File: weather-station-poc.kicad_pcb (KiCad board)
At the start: 4 copper layers, 165 x 91.2 mm, 136 parts, among them IC1 632723100011, IC2 TCPP01-M12, IC3 USBLC6-2SC6, IC4 BME690, IC5 S2-LPQTR, IC6 BALF-SPI2-01D3, IC7 STSAFA110S8OCD03, J1 Conn_ARM_JTAG_SWD_10, J2 61300311121, J3 61300311121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

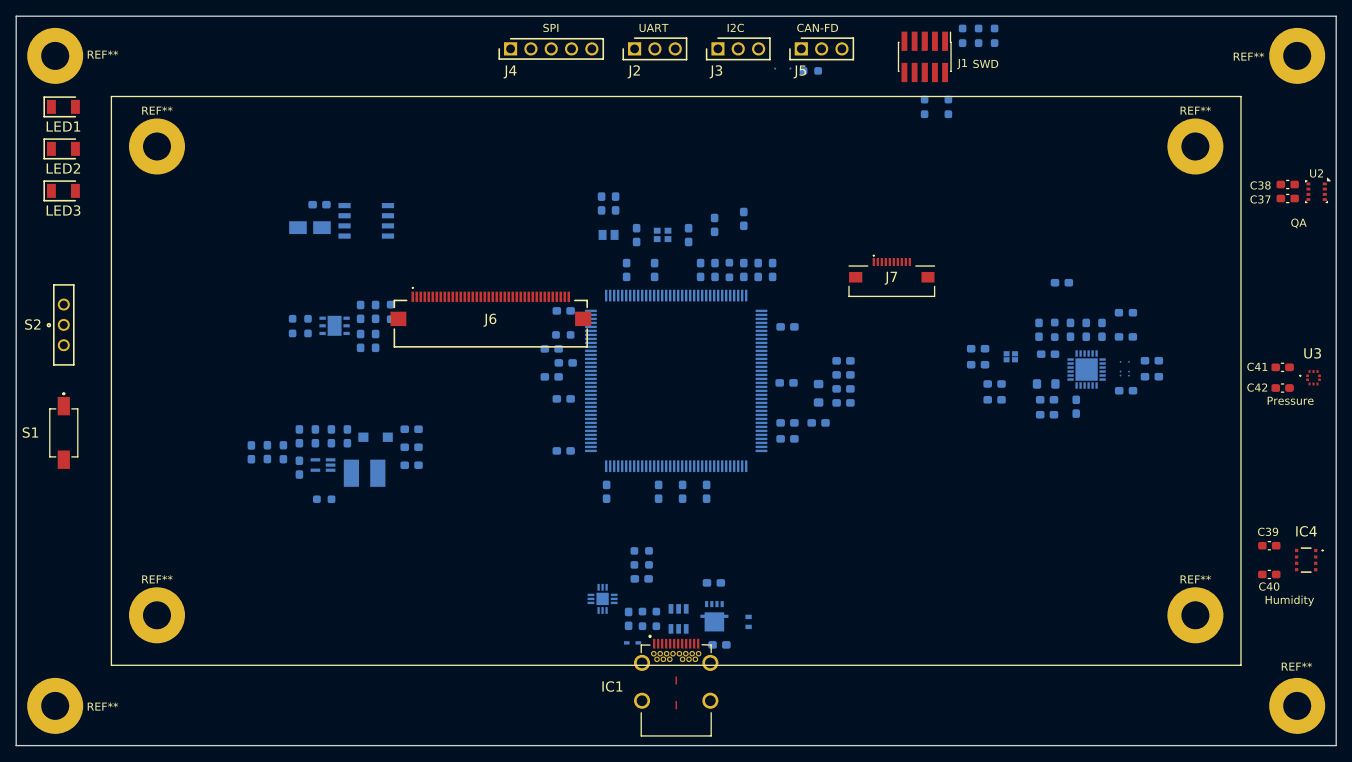
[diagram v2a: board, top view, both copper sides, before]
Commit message: Modify USB data signals name to trace diff pairs
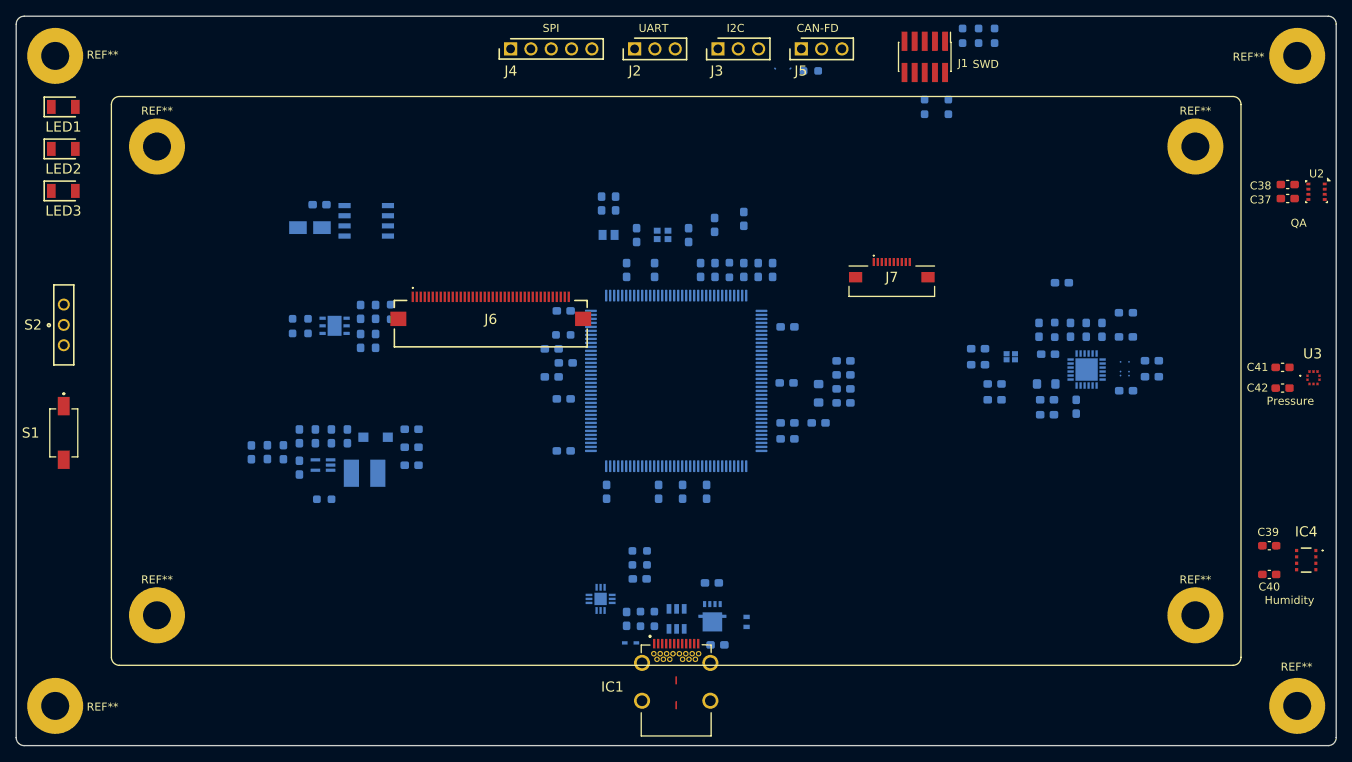
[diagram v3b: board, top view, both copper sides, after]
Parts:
- moved C1 0.25 mm to (141.1, 116.2)
- moved C2 0.25 mm to (150.9, 124.5)
- moved C3 0.25 mm to (150.2, 116.8)
- moved C4 0.25 mm to (139.5, 121.2)
- moved D1 0.25 mm to (154.5, 121.6)
- moved D2 0.25 mm to (140.0, 124.2)
- moved IC2 0.25 mm to (136.2, 118.8)
- moved IC3 0.25 mm to (145.8, 121.2)
- moved Q1 0.25 mm to (150.2, 120.9)
- moved R1 0.25 mm to (143.0, 121.2)
- moved R2 0.25 mm to (141.2, 121.2)
- moved R3 0.25 mm to (141.1, 114.5)
- moved R4 0.25 mm to (141.1, 112.8)
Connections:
- net /MCU/DN_MCU renamed /MCU/MCU_DN
- net /MCU/DP_MCU renamed /MCU/MCU_DP
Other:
- outline, holes or cut-outs redrawn
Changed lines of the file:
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@@
 	(net 41 "Net-(IC2-VBUS_CTRL)")
 	(net 42 "/MCU/~{FLT}_MCU")
-	(net 43 "/MCU/DN_MCU")
-	(net 44 "/MCU/DP_MCU")
+	(net 43 "/MCU/MCU_DN")
+	(net 44 "/MCU/MCU_DP")
 	(net 45 "unconnected-(IC3-VBUS-Pad5)")
 	(net 46 "/Debug-boot/SCL_Debug")
@@
 	(footprint "weather-station-poc-fp:ESDA25P351U1M"
 		(layer "B.Cu")
-		(at 154.75 121.625 -90)
+		(at 154.5 121.625 -90)
 		(descr "1610_2023")
 		(tags "TVS Diode (Uni-directional)")
@@
 	(footprint "weather-station-poc-fp:QFN50P300X300X100-13N-D"
 		(layer "B.Cu")
-		(at 136.5 118.75 -90)
+		(at 136.25 118.75 -90)
 		(descr "QFN12")
 		(tags "Integrated Circuit")
@@
 	(footprint "Capacitor_SMD:C_0603_1608Metric_Pad1.08x0.95mm_HandSolder"
 		(layer "B.Cu")
-		(at 141.3875 116.25 180)
+		(at 141.1375 116.25 180)
 		(descr "Capacitor SMD 0603 (1608 Metric), square (rectangular) end terminal, IPC-7351 nominal with elongated pad for handsoldering. (Body size source: IPC-SM-782 page 76, https://www.pcb-3d.com/wordpress/wp-content/uploads/ipc-sm-782a_amendment_1_and_2.pdf), generated with kicad-footprint-generator")
 		(tags "capacitor handsolder")
@@
 	(footprint "weather-station-poc-fp:STL20N6F7"
 		(layer "B.Cu")
-		(at 150.475 120.925)
+		(at 150.225 120.925)
 		(descr "PowerFLAT™ 3.3x3.3")
 		(tags "MOSFET (N-Channel)")
@@
 	(footprint "Resistor_SMD:R_0603_1608Metric_Pad0.98x0.95mm_HandSolder"
 		(layer "B.Cu")
-		(at 141.3875 114.5)
+		(at 141.1375 114.5)
 		(descr "Resistor SMD 0603 (1608 Metric), square (rectangular) end terminal, IPC-7351 nominal with elongated pad for handsoldering. (Body size source: IPC-SM-782 page 72, https://www.pcb-3d.com/wordpress/wp-content/uploads/ipc-sm-782a_amendment_1_and_2.pdf), generated with kicad-footprint-generator")
 		(tags "resistor handsolder")
@@
 	(footprint "Resistor_SMD:R_0603_1608Metric_Pad0.98x0.95mm_HandSolder"
 		(layer "B.Cu")
-		(at 143.22 121.25 -90)
+		(at 142.97 121.25 -90)
 		(descr "Resistor SMD 0603 (1608 Metric), square (rectangular) end terminal, IPC-7351 nominal with elongated pad for handsoldering. (Body size source: IPC-SM-782 page 72, https://www.pcb-3d.com/wordpress/wp-content/uploads/ipc-sm-782a_amendment_1_and_2.pdf), generated with kicad-footprint-generator")
 		(tags "resistor handsolder")
@@
 	(footprint "weather-station-poc-fp:SODFL1608X70N"
 		(layer "B.Cu")
-		(at 140.245 124.25)
+		(at 139.995 124.25)
 		(descr "SOD-523")
 		(tags "Diode")
@@
 	(footprint "Resistor_SMD:R_0603_1608Metric_Pad0.98x0.95mm_HandSolder"
 		(layer "B.Cu")
-		(at 141.3875 112.75 180)
+		(at 141.1375 112.75 180)
 		(descr "Resistor SMD 0603 (1608 Metric), square (rectangular) end terminal, IPC-7351 nominal with elongated pad for handsoldering. (Body size source: IPC-SM-782 page 72, https://www.pcb-3d.com/wordpress/wp-content/uploads/ipc-sm-782a_amendment_1_and_2.pdf), generated with kicad-footprint-generator")
 		(tags "resistor handsolder")
@@
 	(footprint "Resistor_SMD:R_0603_1608Metric_Pad0.98x0.95mm_HandSolder"
 		(layer "B.Cu")
-		(at 141.485 121.25 -90)
+		(at 141.235 121.25 -90)
 		(descr "Resistor SMD 0603 (1608 Metric), square (rectangular) end terminal, IPC-7351 nominal with elongated pad for handsoldering. (Body size source: IPC-SM-782 page 72, https://www.pcb-3d.com/wordpress/wp-content/uploads/ipc-sm-782a_amendment_1_and_2.pdf), generated with kicad-footprint-generator")
 		(tags "resistor handsolder")
@@
 			(layers "B.Cu" "B.Mask" "B.Paste")
 			(roundrect_rratio 0.25)
-			(net 43 "/MCU/DN_MCU")
+			(net 43 "/MCU/MCU_DN")
 			(pinfunction "PA11")
 			(pintype "bidirectional")
@@
 			(layers "B.Cu" "B.Mask" "B.Paste")
 			(roundrect_rratio 0.25)
-			(net 44 "/MCU/DP_MCU")
+			(net 44 "/MCU/MCU_DP")
 			(pinfunction "PA12")
 			(pintype "bidirectional")
@@
 	(footprint "Capacitor_SMD:C_0603_1608Metric_Pad1.08x0.95mm_HandSolder"
 		(layer "B.Cu")
-		(at 151.105 124.5)
+		(at 150.855 124.5)
 		(descr "Capacitor SMD 0603 (1608 Metric), square (rectangular) end terminal, IPC-7351 nominal with elongated pad for handsoldering. (Body size source: IPC-SM-782 page 76, https://www.pcb-3d.com/wordpress/wp-content/uploads/ipc-sm-782a_amendment_1_and_2.pdf), generated with kicad-footprint-generator")
 		(tags "capacitor handsolder")
@@
 	(footprint "Capacitor_SMD:C_0603_1608Metric_Pad1.08x0.95mm_HandSolder"
 		(layer "B.Cu")
-		(at 150.4125 116.75)
+		(at 150.1625 116.75)
 		(descr "Capacitor SMD 0603 (1608 Metric), square (rectangular) end terminal, IPC-7351 nominal with elongated pad for handsoldering. (Body size source: IPC-SM-782 page 76, https://www.pcb-3d.com/wordpress/wp-content/uploads/ipc-sm-782a_amendment_1_and_2.pdf), generated with kicad-footprint-generator")
 		(tags "capacitor handsolder")
@@
 	(footprint "Capacitor_SMD:C_0603_1608Metric_Pad1.08x0.95mm_HandSolder"
 		(layer "B.Cu")
-		(at 139.75 121.25 90)
+		(at 139.5 121.25 90)
 		(descr "Capacitor SMD 0603 (1608 Metric), square (rectangular) end terminal, IPC-7351 nominal with elongated pad for handsoldering. (Body size source: IPC-SM-782 page 76, https://www.pcb-3d.com/wordpress/wp-content/uploads/ipc-sm-782a_amendment_1_and_2.pdf), generated with kicad-footprint-generator")
 		(tags "capacitor handsolder")
@@
 	(footprint "weather-station-poc-fp:SOT95P280X145-6N"
 		(layer "B.Cu")
-		(at 146 121.25 90)
+		(at 145.75 121.25 90)
 		(descr "SOT23-6L_1")
 		(tags "Integrated Circuit")
@@
 			(size 0.6 1.2)
 			(layers "B.Cu" "B.Mask" "B.Paste")
-			(net 44 "/MCU/DP_MCU")
+			(net 44 "/MCU/MCU_DP")
 			(pinfunction "I/O2_2")
 			(pintype "passive")
@@
 			(size 0.6 1.2)
 			(layers "B.Cu" "B.Mask" "B.Paste")
-			(net 43 "/MCU/DN_MCU")
+			(net 43 "/MCU/MCU_DN")
 			(pinfunction "I/O1_2")
 			(pintype "passive")
@@
 		)
 	)
-	(gr_rect
-		(start 75.1 55.95)
-		(end 216.3 127.05)
+	(gr_line
+		(start 76.1 55.95)
+		(end 215.3 55.95)
 		(stroke
 			(width 0.1)
-			(type solid)
+			(type default)
+		)
+		(layer "F.SilkS")
+	)
+	(gr_arc
+		(start 215.3 55.95)
+		(mid 216.007107 56.242893)
+		(end 216.3 56.95)
+		(stroke
+			(width 0.1)
+			(type default)
+		)
+		(layer "F.SilkS")
+	)
+	(gr_arc
+		(start 76.1 127.05)
+		(mid 75.392893 126.757107)
+		(end 75.1 126.05)
+		(stroke
+			(width 0.1)
+			(type default)
+		)
+		(layer "F.SilkS")
+	)
+	(gr_line
+		(start 215.3 127.05)
+		(end 76.1 127.05)
+		(stroke
+			(width 0.1)
+			(type default)
+		)
+		(layer "F.SilkS")
+	)
+	(gr_line
+		(start 75.1 126.05)
+		(end 75.1 56.95)
+		(stroke
+			(width 0.1)
+			(type default)
+		)
+		(layer "F.SilkS")
+	)
+	(gr_line
+		(start 216.3 56.95)
+		(end 216.3 126.05)
+		(stroke
+			(width 0.1)
+			(type default)
+		)
+		(layer "F.SilkS")
+	)
+	(gr_arc
+		(start 216.3 126.05)
+		(mid 216.007107 126.757107)
+		(end 215.3 127.05)
+		(stroke
+			(width 0.1)
+			(type default)
+		)
+		(layer "F.SilkS")
+	)
+	(gr_arc
+		(start 75.1 56.95)
+		(mid 75.392893 56.242893)
+		(end 76.1 55.95)
+		(stroke
+			(width 0.1)
+			(type default)
 		)
-		(fill no)
 		(layer "F.SilkS")
 	)
@@
 		(layer "Dwgs.User")
 	)
-	(gr_rect
-		(start 63.2 45.9125)
-		(end 228.2 137.0875)
+	(gr_line
+		(start 64.2 45.9125)
+		(end 227.2 45.9125)
 		(stroke
 			(width 0.05)
-			(type solid)
+			(type default)
+		)
+		(layer "Edge.Cuts")
+	)
+	(gr_arc
+		(start 64.2 137.0875)
+		(mid 63.492893 136.794607)
+		(end 63.2 136.0875)
+		(stroke
+			(width 0.05)
+			(type default)
+		)
+		(layer "Edge.Cuts")
+	)
+	(gr_arc
+		(start 63.2 46.9125)
+		(mid 63.492893 46.205393)
+		(end 64.2 45.9125)
+		(stroke
+			(width 0.05)
+			(type default)
+		)
+		(layer "Edge.Cuts")
+	)
+	(gr_line
+		(start 63.2 136.0875)
+		(end 63.2 46.9125)
+		(stroke
+			(width 0.05)
+			(type default)
+		)
+		(layer "Edge.Cuts")
+	)
+	(gr_arc
+		(start 228.2 136.0875)
+		(mid 227.907107 136.794607)
+		(end 227.2 137.0875)
+		(stroke
+			(width 0.05)
+			(type default)
+		)
+		(layer "Edge.Cuts")
+	)
+	(gr_line
+		(start 227.2 137.0875)
+		(end 64.2 137.0875)
+		(stroke
+			(width 0.05)
+			(type default)
+		)
+		(layer "Edge.Cuts")
+	)
+	(gr_line
+		(start 228.2 46.9125)
+		(end 228.2 136.0875)
+		(stroke
+			(width 0.05)
+			(type default)
+		)
+		(layer "Edge.Cuts")
+	)
+	(gr_arc
+		(start 227.2 45.9125)
+		(mid 227.907107 46.205393)
+		(end 228.2 46.9125)
+		(stroke
+			(width 0.05)
+			(type default)
 		)
-		(fill no)
 		(layer "Edge.Cuts")
 	)

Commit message: Add mounting holes with pads in schematic and place it into pcb
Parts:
- removed REF** (x8): MountingHole_3.5mm_Pad, MountingHole:MountingHole_3.5mm_Pad
- added H1: MountingHole_Pad, MountingHole:MountingHole_3.5mm_Pad, F.Cu at (68.1, 50.9)
- added H2: MountingHole_Pad, MountingHole:MountingHole_3.5mm_Pad, F.Cu at (223.3, 50.9)
- added H3: MountingHole_Pad, MountingHole:MountingHole_3.5mm_Pad, F.Cu at (68.1, 132.1)
- added H4: MountingHole_Pad, MountingHole:MountingHole_3.5mm_Pad, F.Cu at (223.3, 132.1)
- added H5: MountingHole_Pad, MountingHole:MountingHole_3.5mm_Pad, F.Cu at (80.8, 62.2)
- added H6: MountingHole_Pad, MountingHole:MountingHole_3.5mm_Pad, F.Cu at (210.6, 62.2)
- added H7: MountingHole_Pad, MountingHole:MountingHole_3.5mm_Pad, F.Cu at (80.8, 120.8)
- added H8: MountingHole_Pad, MountingHole:MountingHole_3.5mm_Pad, F.Cu at (210.6, 120.8)
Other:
- board text added: "Boot"
- board text added: "Reset"
- board text added: "USB C - Data and power"
